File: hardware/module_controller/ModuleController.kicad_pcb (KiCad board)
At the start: 2 copper layers, 60 x 90 mm, 24 parts, among them J1 JST05_StepperMotor, J6 Conn_02x08_Top_Bottom, U1 ULN2003, U2 A1101ELHL, U3 SN75176AP, U4 ATmega8A-A, Y1 16MHz

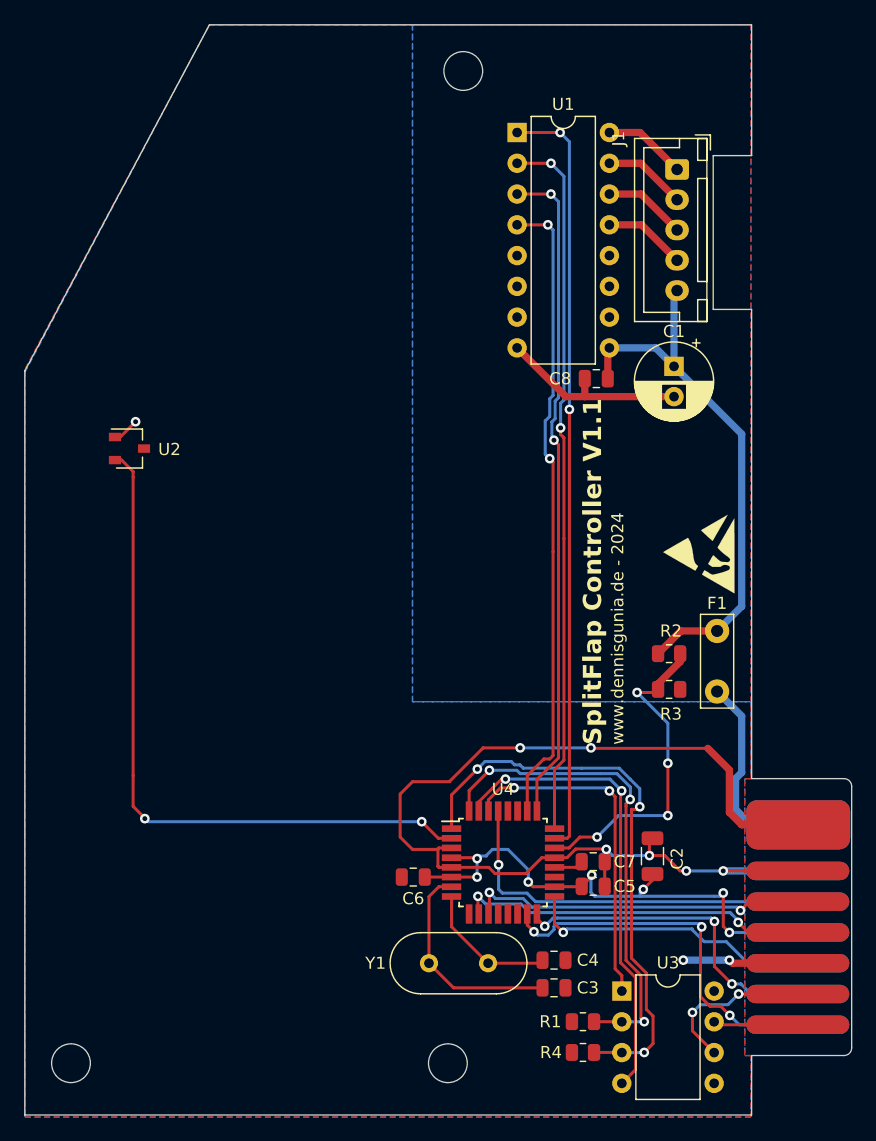
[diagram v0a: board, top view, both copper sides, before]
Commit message: updated schematics
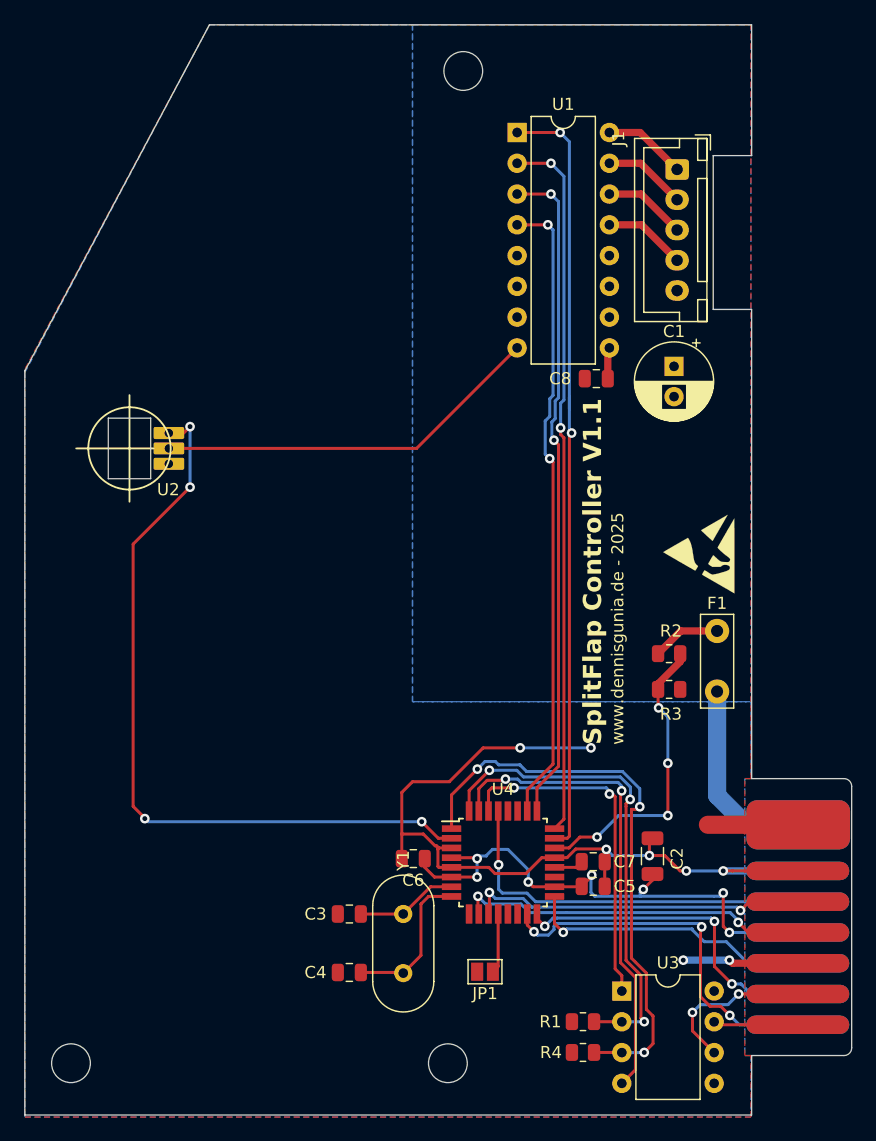
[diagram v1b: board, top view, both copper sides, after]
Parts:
- added JP1: Jumper Addr-Reset, Jumper:SolderJumper-2_P1.3mm_Open_Pad1.0x1.5mm, F.Cu at (124.3, 115.0)
- F1: value Polyfuse 10ma/20mA -> RXEF010
- J1: value JST05_StepperMotor -> JST B5B-XH-A
- J6: value Conn_02x08_Top_Bottom -> 2x08 Edge Connector
- U2: value A1101ELHL -> A1101; footprint Package_TO_SOT_SMD:SOT-23W -> Dennis:UA A1101
- Y1: value 16MHz -> 16,0000-HC49U-S
- moved C3 18.0 mm to (113.2, 110.2), turned to 0 degrees
- moved C4 16.9 mm to (113.2, 115.1), turned to 0 degrees
- moved Y1 4.58 mm to (117.6, 110.2), turned to -90 degrees
- moved U2 3.25 mm to (98.2, 71.8)
- moved C6 1.52 mm to (118.4, 105.7)
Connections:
- U2 pad 2: /GATE_HOME -> GND
- U2 pad 3: GND -> /GATE_HOME
- U4 pad 12: unconnected-(U4-PB0-Pad12) -> Net-(JP1-A)
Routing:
- net +12V: track 45.9 -> 8.96 mm
- net Net-(U4-PB6/XTAL1): track 17.9 -> 8.42 mm
- net /GATE_HOME: track 56.9 -> 62.7 mm, vias 2 -> 4
- net Net-(JP1-A): track 0.00 -> 4.95 mm
- net Net-(J6-Pin_15): track 20.7 -> 16.6 mm
- net GND: track 116.8 -> 120.4 mm
- net Net-(U4-ADC7): track 27.2 -> 25.3 mm
- net Net-(U4-PB7/XTAL2): track 11.4 -> 12.6 mm
- net +5V: track 47.1 -> 46.0 mm, vias 8 -> 7
- net /MOT_A: track 63.3 -> 64.4 mm
- net /BUS_TX: track 38.9 -> 39.8 mm
- net /BUS_RX: track 28.4 -> 28.9 mm
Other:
- board text added: "www.dennisgunia.de - 2025"
- board text removed: "www.dennisgunia.de - 2024"
